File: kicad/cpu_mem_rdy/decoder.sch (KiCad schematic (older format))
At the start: 26 parts, among them P2 CONN_01X08, U11 74LS273, U12 74LS244, U14 GAL16V8, U5 GAL22V10, U9 74LS139

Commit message: cleanup routing, micro usb jack
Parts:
- C11, C12, C13: footprint Capacitors_ThroughHole:C_Rect_L4_W2.5_P2.5 -> Discret:C1
- U11, U12: footprint Housings_DIP:DIP-20_W7.62mm_LongPads -> Sockets_DIP:DIP-20__300_ELL
- U5: footprint Housings_DIP:DIP-24_W7.62mm_LongPads -> Sockets_DIP:DIP-24__300_ELL
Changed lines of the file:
@@
 LIBS:xo-14s
 LIBS:osc
+LIBS:cpu_mem_rdy-cache
 EELAYER 25 0
 EELAYER END
@@
 F 0 "U5" H 1900 6800 60  0000 C CNN
 F 1 "GAL22V10" H 1900 5300 60  0000 C CNN
-F 2 "Housings_DIP:DIP-24_W7.62mm_LongPads" H 1850 6050 60  0001 C CNN
+F 2 "Sockets_DIP:DIP-24__300_ELL" H 1850 6050 60  0001 C CNN
 F 3 "" H 1850 6050 60  0000 C CNN
 	1    1850 6050
@@
 $EndComp
 $Comp
-L GND #PWR027
+L GND #PWR028
 U 1 1 544D50D2
 P 1550 6900
-F 0 "#PWR027" H 1550 6900 30  0001 C CNN
+F 0 "#PWR028" H 1550 6900 30  0001 C CNN
 F 1 "GND" H 1550 6830 30  0001 C CNN
 F 2 "" H 1550 6900 60  0000 C CNN
@@
 $EndComp
 $Comp
-L VCC #PWR028
+L VCC #PWR029
 U 1 1 544D50D8
 P 1550 5200
-F 0 "#PWR028" H 1550 5300 30  0001 C CNN
+F 0 "#PWR029" H 1550 5300 30  0001 C CNN
 F 1 "VCC" H 1550 5300 30  0000 C CNN
 F 2 "" H 1550 5200 60  0000 C CNN
@@
 A15
 $Comp
-L VCC #PWR029
+L VCC #PWR030
 U 1 1 544D6887
 P 950 5350
-F 0 "#PWR029" H 950 5450 30  0001 C CNN
+F 0 "#PWR030" H 950 5450 30  0001 C CNN
 F 1 "VCC" H 950 5450 30  0000 C CNN
 F 2 "" H 950 5350 60  0000 C CNN
@@
 A4
 $Comp
-L VCC #PWR030
+L VCC #PWR031
 U 1 1 544D68A5
 P 1250 3850
-F 0 "#PWR030" H 1250 3950 30  0001 C CNN
+F 0 "#PWR031" H 1250 3950 30  0001 C CNN
 F 1 "VCC" H 1250 3950 30  0000 C CNN
 F 2 "" H 1250 3850 60  0000 C CNN
@@
 $EndComp
 $Comp
-L GND #PWR031
+L GND #PWR032
 U 1 1 544D68AB
 P 1250 4850
-F 0 "#PWR031" H 1250 4850 30  0001 C CNN
+F 0 "#PWR032" H 1250 4850 30  0001 C CNN
 F 1 "GND" H 1250 4780 30  0001 C CNN
 F 2 "" H 1250 4850 60  0000 C CNN
@@
 /CS_IO3
 $Comp
-L VCC #PWR032
+L VCC #PWR033
 U 1 1 544D6F18
 P 6750 4500
-F 0 "#PWR032" H 6750 4600 30  0001 C CNN
+F 0 "#PWR033" H 6750 4600 30  0001 C CNN
 F 1 "VCC" H 6750 4600 30  0000 C CNN
 F 2 "" H 6750 4500 60  0000 C CNN
@@
 $EndComp
 $Comp
-L GND #PWR033
+L GND #PWR034
 U 1 1 544D700F
 P 6750 5950
-F 0 "#PWR033" H 6750 5950 30  0001 C CNN
+F 0 "#PWR034" H 6750 5950 30  0001 C CNN
 F 1 "GND" H 6750 5880 30  0001 C CNN
 F 2 "" H 6750 5950 60  0000 C CNN
@@
 $EndComp
 $Comp
-L VCC #PWR034
+L VCC #PWR035
 U 1 1 544E9402
 P 5800 6600
-F 0 "#PWR034" H 5800 6700 30  0001 C CNN
+F 0 "#PWR035" H 5800 6700 30  0001 C CNN
 F 1 "VCC" H 5800 6700 30  0000 C CNN
 F 2 "" H 5800 6600 60  0000 C CNN
@@
 $EndComp
 $Comp
-L GND #PWR035
+L GND #PWR036
 U 1 1 544E9408
 P 5800 7150
-F 0 "#PWR035" H 5800 7150 30  0001 C CNN
+F 0 "#PWR036" H 5800 7150 30  0001 C CNN
 F 1 "GND" H 5800 7080 30  0001 C CNN
 F 2 "" H 5800 7150 60  0000 C CNN
@@
 F 0 "C11" H 5800 6950 40  0000 L CNN
 F 1 "100n" H 5806 6765 40  0000 L CNN
-F 2 "Capacitors_ThroughHole:C_Rect_L4_W2.5_P2.5" H 5838 6700 30  0001 C CNN
+F 2 "Discret:C1" H 5838 6700 30  0001 C CNN
 F 3 "" H 5800 6850 60  0000 C CNN
 	1    5800 6850
@@
 F 0 "C12" H 6050 6950 40  0000 L CNN
 F 1 "100n" H 6056 6765 40  0000 L CNN
-F 2 "Capacitors_ThroughHole:C_Rect_L4_W2.5_P2.5" H 6088 6700 30  0001 C CNN
+F 2 "Discret:C1" H 6088 6700 30  0001 C CNN
 F 3 "" H 6050 6850 60  0000 C CNN
 	1    6050 6850
@@
 F 0 "C13" H 6300 6950 40  0000 L CNN
 F 1 "100n" H 6306 6765 40  0000 L CNN
-F 2 "Capacitors_ThroughHole:C_Rect_L4_W2.5_P2.5" H 6338 6700 30  0001 C CNN
+F 2 "Discret:C1" H 6338 6700 30  0001 C CNN
 F 3 "" H 6300 6850 60  0000 C CNN
 	1    6300 6850
@@
 $EndComp
 $Comp
-L VCC #PWR036
+L VCC #PWR037
 U 1 1 548A1DBF
 P 9450 4500
-F 0 "#PWR036" H 9450 4600 30  0001 C CNN
+F 0 "#PWR037" H 9450 4600 30  0001 C CNN
 F 1 "VCC" H 9450 4600 30  0000 C CNN
 F 2 "" H 9450 4500 60  0000 C CNN
@@
 $EndComp
 $Comp
-L GND #PWR037
+L GND #PWR038
 U 1 1 548A1EB2
 P 9450 5950
-F 0 "#PWR037" H 9450 5950 30  0001 C CNN
+F 0 "#PWR038" H 9450 5950 30  0001 C CNN
 F 1 "GND" H 9450 5880 30  0001 C CNN
 F 2 "" H 9450 5950 60  0000 C CNN
@@
 F 0 "U11" H 7050 5050 60  0000 C CNN
 F 1 "74LS273" H 7050 4850 60  0000 C CNN
-F 2 "Housings_DIP:DIP-20_W7.62mm_LongPads" H 7050 5200 60  0001 C CNN
+F 2 "Sockets_DIP:DIP-20__300_ELL" H 7050 5200 60  0001 C CNN
 F 3 "" H 7050 5200 60  0000 C CNN
 	1    7050 5200
@@
 F 0 "U12" H 9500 5000 60  0000 C CNN
 F 1 "74LS244" H 9550 4800 60  0000 C CNN
-F 2 "Housings_DIP:DIP-20_W7.62mm_LongPads" H 9450 5200 60  0001 C CNN
+F 2 "Sockets_DIP:DIP-20__300_ELL" H 9450 5200 60  0001 C CNN
 F 3 "" H 9450 5200 60  0000 C CNN
 	1    9450 5200
@@
 $EndComp
 $Comp
-L GND #PWR038
+L GND #PWR039
 U 1 1 54C3A7FA
 P 9900 4200
-F 0 "#PWR038" H 9900 4200 30  0001 C CNN
+F 0 "#PWR039" H 9900 4200 30  0001 C CNN
 F 1 "GND" H 9900 4130 30  0001 C CNN
 F 2 "" H 9900 4200 60  0000 C CNN
@@
 Connection ~ 3100 4050
 $Comp
-L GND #PWR039
+L GND #PWR040
 U 1 1 56AAAA8A
 P 3700 7650
-F 0 "#PWR039" H 3700 7650 30  0001 C CNN
+F 0 "#PWR040" H 3700 7650 30  0001 C CNN
 F 1 "GND" H 3700 7580 30  0001 C CNN
 F 2 "" H 3700 7650 60  0000 C CNN

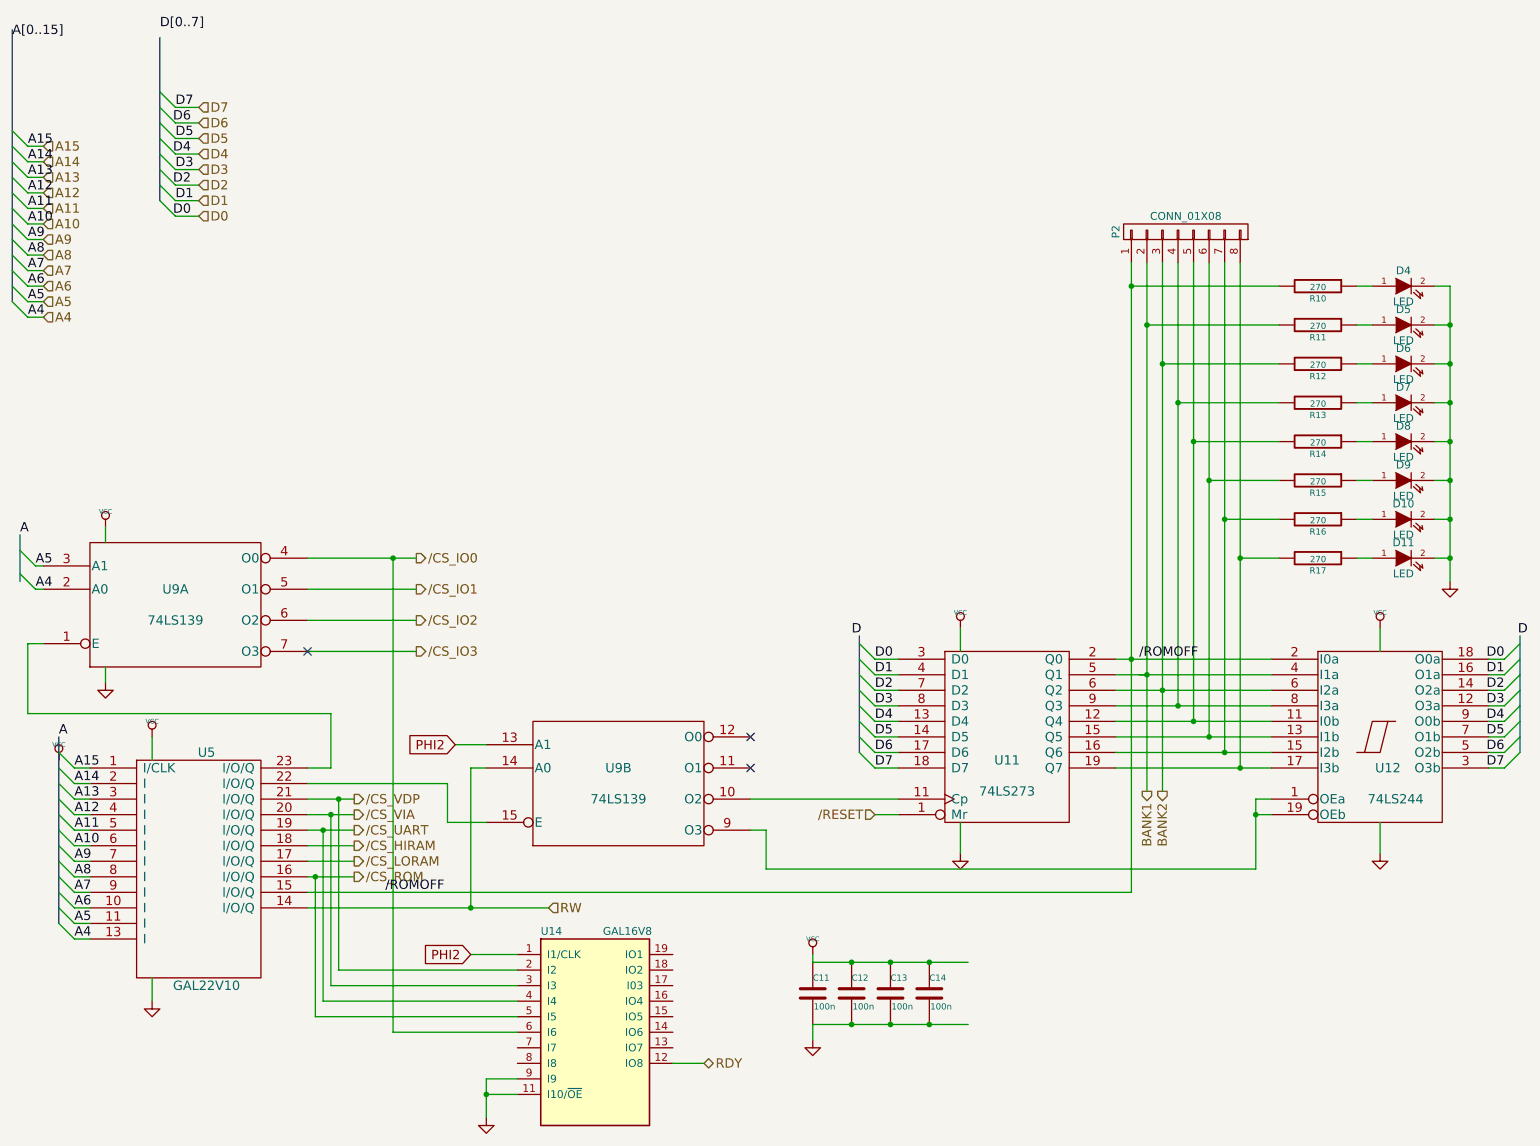
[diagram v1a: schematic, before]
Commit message: no rdy for via, io1-3 connected to rdygen
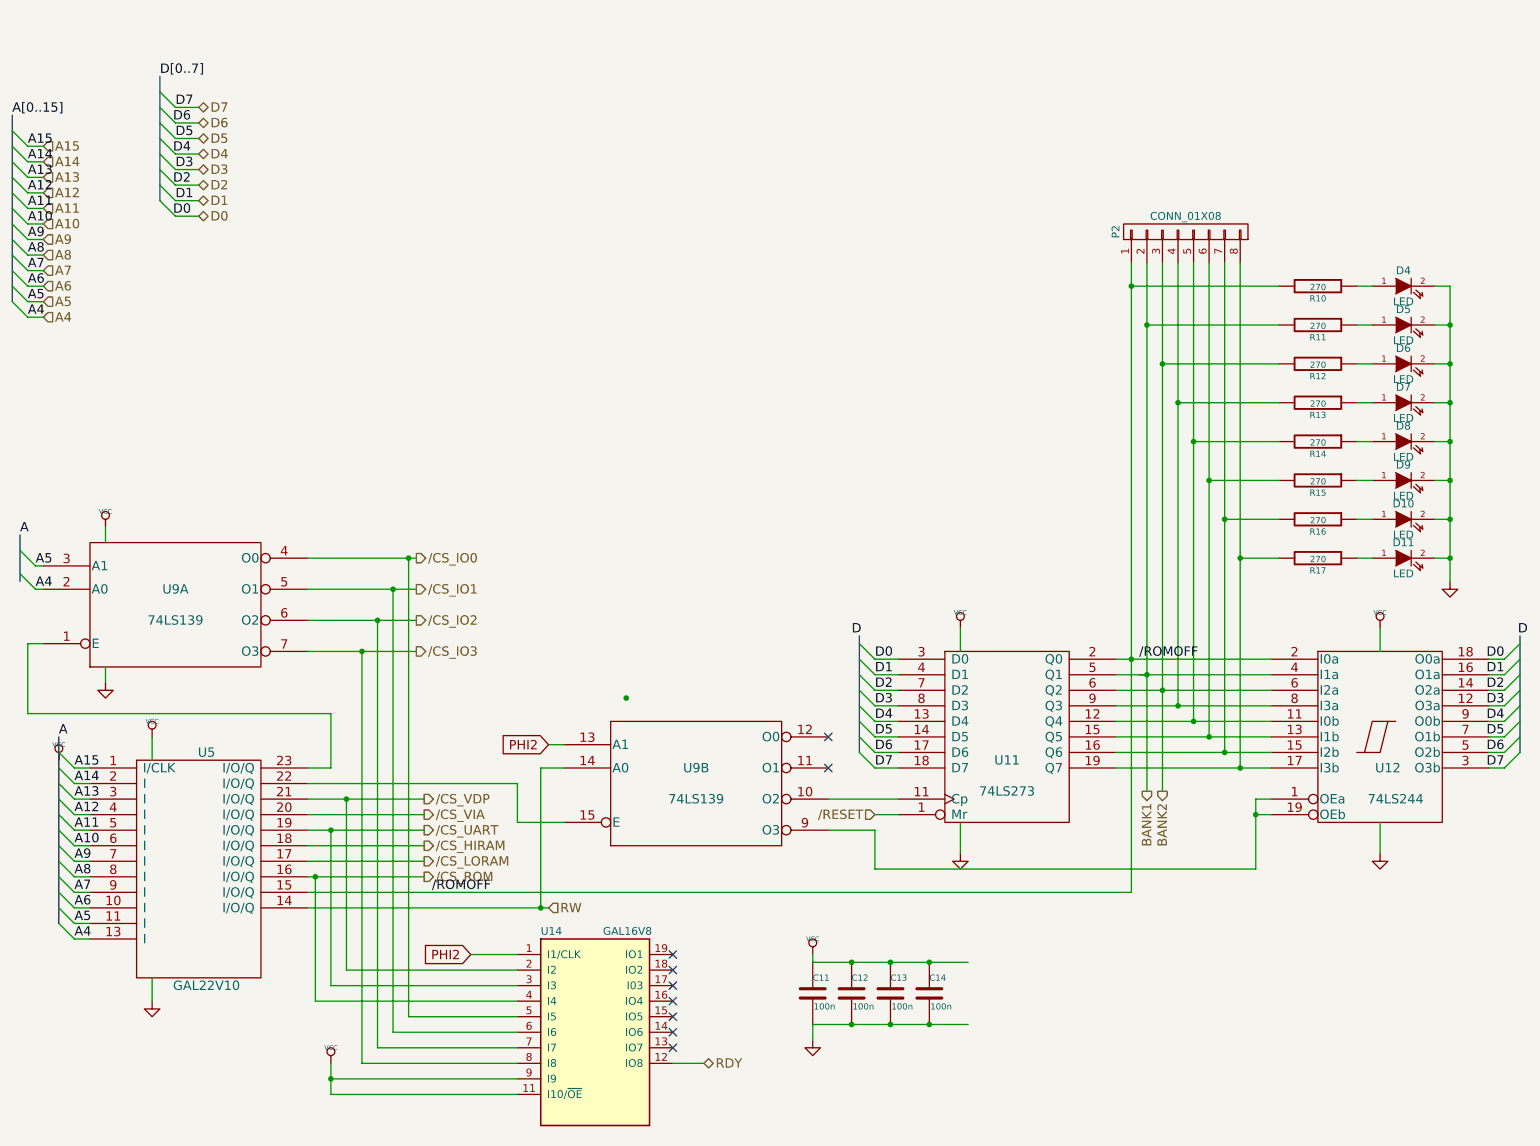
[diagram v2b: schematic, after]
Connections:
- net /CS_IO0: now also U14.5 (I5); no longer U14.6 (I6)
- net /CS_IO1: now also U14.6 (I6)
- net /CS_IO2: now also U14.7 (I7)
- net /CS_IO3: now also U14.8 (I8)
- net /CS_ROM: now also U14.4 (I4); no longer U14.5 (I5)
- net /CS_UART: now also U14.3 (I3); no longer U14.4 (I4)
- net /CS_VIA: no longer U14.3 (I3)
- net GND: no longer U14.11 (I10/~OE~), U14.9 (I9)
- net VCC: now also U14.11 (I10/~OE~), U14.9 (I9)
- no-connect marks 3 -> 9
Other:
- moved on the sheet: U9B
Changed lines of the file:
@@
 Entry Wire Line
 	650  2400 750  2500
-Text Label 650  700  0    60   ~ 0
+Text Label 650  1200 0    60   ~ 0
 A[0..15]
 Entry Wire Line
@@
 Text Label 1700 1750 0    60   ~ 0
 D1
-Text Label 1600 650  0    60   ~ 0
+Text Label 1600 950  0    60   ~ 0
 D[0..7]
 Entry Wire Line
@@
 Text Label 1800 1850 2    60   ~ 0
 D0
-Text HLabel 1850 1850 2    60   Input ~ 0
+Text HLabel 1850 1850 2    60   BiDi ~ 0
 D0
-Text HLabel 1850 1750 2    60   Input ~ 0
+Text HLabel 1850 1750 2    60   BiDi ~ 0
 D1
-Text HLabel 1850 1650 2    60   Input ~ 0
+Text HLabel 1850 1650 2    60   BiDi ~ 0
 D2
-Text HLabel 1850 1550 2    60   Input ~ 0
+Text HLabel 1850 1550 2    60   BiDi ~ 0
 D3
-Text HLabel 1850 1450 2    60   Input ~ 0
+Text HLabel 1850 1450 2    60   BiDi ~ 0
 D4
-Text HLabel 1850 1350 2    60   Input ~ 0
+Text HLabel 1850 1350 2    60   BiDi ~ 0
 D5
-Text HLabel 1850 1250 2    60   Input ~ 0
+Text HLabel 1850 1250 2    60   BiDi ~ 0
 D6
-Text HLabel 1850 1150 2    60   Input ~ 0
+Text HLabel 1850 1150 2    60   BiDi ~ 0
 D7
 Text Label 750  2500 0    60   ~ 0
@@
 	1    0    0    -1
 $EndComp
-NoConn ~ 2550 4650
 Text Label 700  3900 0    60   ~ 0
 A
-Text HLabel 2850 6100 2    60   Output ~ 0
+Text HLabel 3300 6100 2    60   Output ~ 0
 /CS_ROM
-Text HLabel 2850 6000 2    60   Output ~ 0
+Text HLabel 3300 6000 2    60   Output ~ 0
 /CS_LORAM
-Text HLabel 2850 5900 2    60   Output ~ 0
+Text HLabel 3300 5900 2    60   Output ~ 0
 /CS_HIRAM
 Text HLabel 4100 6300 2    60   Input ~ 0
 RW
-Text HLabel 2850 5800 2    60   Output ~ 0
+Text HLabel 3300 5800 2    60   Output ~ 0
 /CS_UART
-Text HLabel 2850 5700 2    60   Output ~ 0
+Text HLabel 3300 5700 2    60   Output ~ 0
 /CS_VIA
-Text HLabel 2850 5600 2    60   Output ~ 0
+Text HLabel 3300 5600 2    60   Output ~ 0
 /CS_VDP
 Text HLabel 3250 4050 2    60   Output ~ 0
@@
 Text Label 7900 4700 0    60   ~ 0
 /ROMOFF
-Text Label 3050 6200 0    60   ~ 0
+Text Label 3350 6200 0    60   ~ 0
 /ROMOFF
 $Comp
 L 74LS139 U9
 U 2 1 548A0B1E
-P 4550 5500
-F 0 "U9" H 4550 5600 60  0000 C CNN
-F 1 "74LS139" H 4550 5400 60  0000 C CNN
-F 2 "Housings_DIP:DIP-16_W7.62mm_LongPads" H 4550 5500 60  0001 C CNN
-F 3 "" H 4550 5500 60  0000 C CNN
-	2    4550 5500
+P 5050 5500
+F 0 "U9" H 5050 5600 60  0000 C CNN
+F 1 "74LS139" H 5050 5400 60  0000 C CNN
+F 2 "Housings_DIP:DIP-16_W7.62mm_LongPads" H 5050 5500 60  0001 C CNN
+F 3 "" H 5050 5500 60  0000 C CNN
+	2    5050 5500
 	1    0    0    -1
 $EndComp
@@
 	1    0    0    -1
 $EndComp
-Text GLabel 3500 5250 0    60   Input ~ 0
+Text GLabel 4100 5250 0    60   Input ~ 0
 PHI2
-NoConn ~ 5400 5400
+NoConn ~ 5900 5400
 Text HLabel 6200 5700 0    60   Input ~ 0
 /RESET
@@
 	7850 6200 2550 6200
 Wire Wire Line
-	2550 6100 2850 6100
-Wire Wire Line
-	2550 6000 2850 6000
-Wire Wire Line
-	2550 5900 2850 5900
-Wire Wire Line
-	2550 5800 2850 5800
-Wire Wire Line
-	2550 5700 2850 5700
-Wire Wire Line
-	2550 5600 2850 5600
+	2550 6100 3300 6100
+Wire Wire Line
+	2550 6000 3300 6000
+Wire Wire Line
+	2550 5900 3300 5900
+Wire Wire Line
+	2550 5800 3300 5800
+Wire Wire Line
+	2550 5700 3300 5700
+Wire Wire Line
+	2550 5600 3300 5600
 Wire Bus Line
 	6100 4550 6100 5300
@@
 	750  2500 850  2500
 Wire Bus Line
-	650  650  650  2400
-Wire Bus Line
-	1600 700  1600 1750
+	1600 950  1600 1750
 Wire Wire Line
 	1700 1150 1850 1150
@@
 	10250 5400 10150 5400
 Wire Wire Line
-	3450 5500 3450 5750
-Wire Wire Line
-	2550 5500 3450 5500
+	3900 5500 3900 5750
+Wire Wire Line
+	2550 5500 3900 5500
 Wire Wire Line
 	7850 2150 7850 6200
@@
 Connection ~ 8550 5400
 Wire Wire Line
-	3450 5750 3700 5750
-Wire Wire Line
-	3700 5250 3500 5250
+	3900 5750 4200 5750
+Wire Wire Line
+	4200 5250 4100 5250
 Wire Wire Line
 	9450 4500 9450 4650
@@
 	9450 5750 9450 5950
 Wire Wire Line
-	3700 5400 3600 5400
-Wire Wire Line
-	3600 5400 3600 6300
-Connection ~ 3600 6300
-Wire Wire Line
-	5500 5800 5500 6050
-Wire Wire Line
-	5500 6050 8650 6050
+	4200 5400 4050 5400
+Wire Wire Line
+	4050 5400 4050 6300
+Connection ~ 4050 6300
+Wire Wire Line
+	6200 5800 6200 6050
+Wire Wire Line
+	8650 6050 6200 6050
 Wire Wire Line
 	8750 5600 8650 5600
@@
 Connection ~ 8650 5700
 Wire Wire Line
-	5500 5800 5400 5800
-Wire Wire Line
-	5400 5600 6350 5600
+	6200 5800 5900 5800
+Wire Wire Line
+	5900 5600 6350 5600
 Wire Wire Line
 	6200 5700 6350 5700
@@
 Wire Wire Line
 	9800 4050 9900 4050
-NoConn ~ 5400 5200
+NoConn ~ 5900 5200
 $Comp
 L GAL16V8 U14
@@
 	3600 6600 3900 6600
 Wire Wire Line
-	2700 6800 2700 5700
-Connection ~ 2700 5700
-Wire Wire Line
-	2650 6900 2650 5800
-Connection ~ 2650 5800
-Wire Wire Line
-	2750 6700 2750 5600
-Connection ~ 2750 5600
+	2700 6800 2700 5800
+Connection ~ 2700 5800
+Wire Wire Line
+	2800 6700 2800 5600
+Connection ~ 2800 5600
 Wire Wire Line
 	2550 4050 3250 4050
 Wire Wire Line
-	3100 7100 3100 4050
-Connection ~ 3100 4050
-$Comp
-L GND #PWR040
-U 1 1 56AAAA8A
-P 3700 7650
-F 0 "#PWR040" H 3700 7650 30  0001 C CNN
-F 1 "GND" H 3700 7580 30  0001 C CNN
-F 2 "" H 3700 7650 60  0000 C CNN
-F 3 "" H 3700 7650 60  0000 C CNN
-	1    3700 7650
-	1    0    0    -1
-$EndComp
-Wire Wire Line
-	3700 7400 3700 7650
-Wire Wire Line
-	3700 7400 3900 7400
-Wire Wire Line
-	3900 7500 3700 7500
-Connection ~ 3700 7500
+	3200 7000 3200 4050
+Connection ~ 3200 4050
+Wire Wire Line
+	2700 7400 3900 7400
+Wire Wire Line
+	2700 7500 3900 7500
 Text HLabel 5100 7300 2    60   3State ~ 0
 RDY
@@
 $EndComp
 Wire Wire Line
-	2750 6700 3900 6700
-Wire Wire Line
-	2700 6800 3900 6800
-Wire Wire Line
-	2650 6900 3900 6900
-Wire Wire Line
-	3900 7000 2600 7000
-Wire Wire Line
-	2600 7000 2600 6100
+	2800 6700 3900 6700
+Wire Wire Line
+	2600 6900 2600 6100
 Connection ~ 2600 6100
-Wire Wire Line
-	3100 7100 3900 7100
 Connection ~ 6550 6650
 Connection ~ 6550 7050
+Wire Bus Line
+	650  1200 650  2400
+Wire Wire Line
+	3100 7100 3100 4250
+Connection ~ 3100 4250
+Wire Wire Line
+	3000 7200 3000 4450
+Connection ~ 3000 4450
+$Comp
+L VCC #PWR040
+U 1 1 56B9A31D
+P 2700 7300
+F 0 "#PWR040" H 2700 7400 30  0001 C CNN
+F 1 "VCC" H 2700 7400 30  0000 C CNN
+F 2 "" H 2700 7300 60  0000 C CNN
+F 3 "" H 2700 7300 60  0000 C CNN
+	1    2700 7300
+	1    0    0    -1
+$EndComp
+Wire Wire Line
+	2700 7300 2700 7500
+Connection ~ 2700 7400
+Connection ~ 4600 4950
+Wire Wire Line
+	2700 6800 3900 6800
+Wire Wire Line
+	3900 6900 2600 6900
+Wire Wire Line
+	3200 7000 3900 7000
+Wire Wire Line
+	3100 7100 3900 7100
+Wire Wire Line
+	3000 7200 3900 7200
+Wire Wire Line
+	3900 7300 2900 7300
+Wire Wire Line
+	2900 7300 2900 4650
+Connection ~ 2900 4650
+NoConn ~ 4900 7200
+NoConn ~ 4900 7100
+NoConn ~ 4900 7000
+NoConn ~ 4900 6900
+NoConn ~ 4900 6800
+NoConn ~ 4900 6700
+NoConn ~ 4900 6600
 $EndSCHEMATC

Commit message: USB B for power
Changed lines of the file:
@@
 $EndComp
 $Comp
-L GND #PWR028
+L GND #PWR027
 U 1 1 544D50D2
 P 1550 6900
-F 0 "#PWR028" H 1550 6900 30  0001 C CNN
+F 0 "#PWR027" H 1550 6900 30  0001 C CNN
 F 1 "GND" H 1550 6830 30  0001 C CNN
 F 2 "" H 1550 6900 60  0000 C CNN
@@
 $EndComp
 $Comp
-L VCC #PWR029
+L VCC #PWR028
 U 1 1 544D50D8
 P 1550 5200
-F 0 "#PWR029" H 1550 5300 30  0001 C CNN
+F 0 "#PWR028" H 1550 5300 30  0001 C CNN
 F 1 "VCC" H 1550 5300 30  0000 C CNN
 F 2 "" H 1550 5200 60  0000 C CNN
@@
 A15
 $Comp
-L VCC #PWR030
+L VCC #PWR029
 U 1 1 544D6887
 P 950 5350
-F 0 "#PWR030" H 950 5450 30  0001 C CNN
+F 0 "#PWR029" H 950 5450 30  0001 C CNN
 F 1 "VCC" H 950 5450 30  0000 C CNN
 F 2 "" H 950 5350 60  0000 C CNN
@@
 A4
 $Comp
-L VCC #PWR031
+L VCC #PWR030
 U 1 1 544D68A5
 P 1250 3850
-F 0 "#PWR031" H 1250 3950 30  0001 C CNN
+F 0 "#PWR030" H 1250 3950 30  0001 C CNN
 F 1 "VCC" H 1250 3950 30  0000 C CNN
 F 2 "" H 1250 3850 60  0000 C CNN
@@
 $EndComp
 $Comp
-L GND #PWR032
+L GND #PWR031
 U 1 1 544D68AB
 P 1250 4850
-F 0 "#PWR032" H 1250 4850 30  0001 C CNN
+F 0 "#PWR031" H 1250 4850 30  0001 C CNN
 F 1 "GND" H 1250 4780 30  0001 C CNN
 F 2 "" H 1250 4850 60  0000 C CNN
@@
 /CS_IO3
 $Comp
-L VCC #PWR033
+L VCC #PWR032
 U 1 1 544D6F18
 P 6750 4500
-F 0 "#PWR033" H 6750 4600 30  0001 C CNN
+F 0 "#PWR032" H 6750 4600 30  0001 C CNN
 F 1 "VCC" H 6750 4600 30  0000 C CNN
 F 2 "" H 6750 4500 60  0000 C CNN
@@
 $EndComp
 $Comp
-L GND #PWR034
+L GND #PWR033
 U 1 1 544D700F
 P 6750 5950
-F 0 "#PWR034" H 6750 5950 30  0001 C CNN
+F 0 "#PWR033" H 6750 5950 30  0001 C CNN
 F 1 "GND" H 6750 5880 30  0001 C CNN
 F 2 "" H 6750 5950 60  0000 C CNN
@@
 $EndComp
 $Comp
-L VCC #PWR035
+L VCC #PWR034
 U 1 1 544E9402
 P 5800 6600
-F 0 "#PWR035" H 5800 6700 30  0001 C CNN
+F 0 "#PWR034" H 5800 6700 30  0001 C CNN
 F 1 "VCC" H 5800 6700 30  0000 C CNN
 F 2 "" H 5800 6600 60  0000 C CNN
@@
 $EndComp
 $Comp
-L GND #PWR036
+L GND #PWR035
 U 1 1 544E9408
 P 5800 7150
-F 0 "#PWR036" H 5800 7150 30  0001 C CNN
+F 0 "#PWR035" H 5800 7150 30  0001 C CNN
 F 1 "GND" H 5800 7080 30  0001 C CNN
 F 2 "" H 5800 7150 60  0000 C CNN
@@
 $EndComp
 $Comp
-L VCC #PWR037
+L VCC #PWR036
 U 1 1 548A1DBF
 P 9450 4500
-F 0 "#PWR037" H 9450 4600 30  0001 C CNN
+F 0 "#PWR036" H 9450 4600 30  0001 C CNN
 F 1 "VCC" H 9450 4600 30  0000 C CNN
 F 2 "" H 9450 4500 60  0000 C CNN
@@
 $EndComp
 $Comp
-L GND #PWR038
+L GND #PWR037
 U 1 1 548A1EB2
 P 9450 5950
-F 0 "#PWR038" H 9450 5950 30  0001 C CNN
+F 0 "#PWR037" H 9450 5950 30  0001 C CNN
 F 1 "GND" H 9450 5880 30  0001 C CNN
 F 2 "" H 9450 5950 60  0000 C CNN
@@
 $EndComp
 $Comp
-L GND #PWR039
+L GND #PWR038
 U 1 1 54C3A7FA
 P 9900 4200
-F 0 "#PWR039" H 9900 4200 30  0001 C CNN
+F 0 "#PWR038" H 9900 4200 30  0001 C CNN
 F 1 "GND" H 9900 4130 30  0001 C CNN
 F 2 "" H 9900 4200 60  0000 C CNN
@@
 	6200 5800 6200 6050
 Wire Wire Line
-	8650 6050 6200 6050
+	6200 6050 8650 6050
 Wire Wire Line
 	8750 5600 8650 5600
@@
 Connection ~ 3000 4450
 $Comp
-L VCC #PWR040
+L VCC #PWR039
 U 1 1 56B9A31D
 P 2700 7300
-F 0 "#PWR040" H 2700 7400 30  0001 C CNN
+F 0 "#PWR039" H 2700 7400 30  0001 C CNN
 F 1 "VCC" H 2700 7400 30  0000 C CNN
 F 2 "" H 2700 7300 60  0000 C CNN
